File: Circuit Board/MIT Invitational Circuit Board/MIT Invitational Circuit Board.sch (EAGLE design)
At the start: 361 parts, among them IC1101 7805DT, IC1201 7805DT, IC1301 7805DT, IC1501 7805DT, J1005 ICSP_HEADER, J1104 ICSP_HEADER, J1204 ICSP_HEADER, J1304 ICSP_HEADER, J204 ICSP_HEADER, J301 ICSP_HEADER, J401 ICSP_HEADER, J503 ICSP_HEADER, J603 ICSP_HEADER, J703 ICSP_HEADER, J704 ICSP_HEADER, J903 ICSP_HEADER, Q1001 PSMN7R0-60YS, Q1401 PSMN7R0-60YS, Q201 PSMN7R0-60YS, Q301 500mA/300V, Q401 500mA/300V, Q501 PSMN7R0-60YS, Q601 PSMN7R0-60YS, Q801 PSMN7R0-60YS, Q901 PSMN7R0-60YS, U1001 ATTINY25-20SSUR, U1002 MIC5205, U101 74HC1G04, U102 MIC5205, U1101 DRV8835, U1102 ATTINY25-20SSUR, U1201 DRV8835, U1202 ATTINY25-20SSUR, U1301 DRV8835, U1302 ATTINY25-20SSUR, U1401 74HC1G04, U1402 MIC5205, U201 74HC1G04, U202 ATTINY25-20SSUR, U203 MIC5205, U301 74HC1G04, U302 SN74C1G08-DCK, U303 ATTINY25-20SSUR, U304 MIC5205, U401 74HC1G04, U402 SN74C1G08-DCK, U403 ATTINY25-20SSUR, U404 MIC5205, U501 74HC1G04, U502 SN74C1G08-DCK, U503 ATTINY25-20SSUR, U504 MIC5205, U601 74HC1G04, U602 SN74C1G08-DCK, U603 ATTINY25-20SSUR, U604 MIC5205, U701 ATTINY25-20SSUR, U702 ATTINY25-20SSUR, U703 MIC5205, U801 74HC1G04, U802 SN74C1G08-DCK, U803 MIC5205, U901 ATTINY25-20SSUR, U902 MIC5205, X1601 MSTBA2

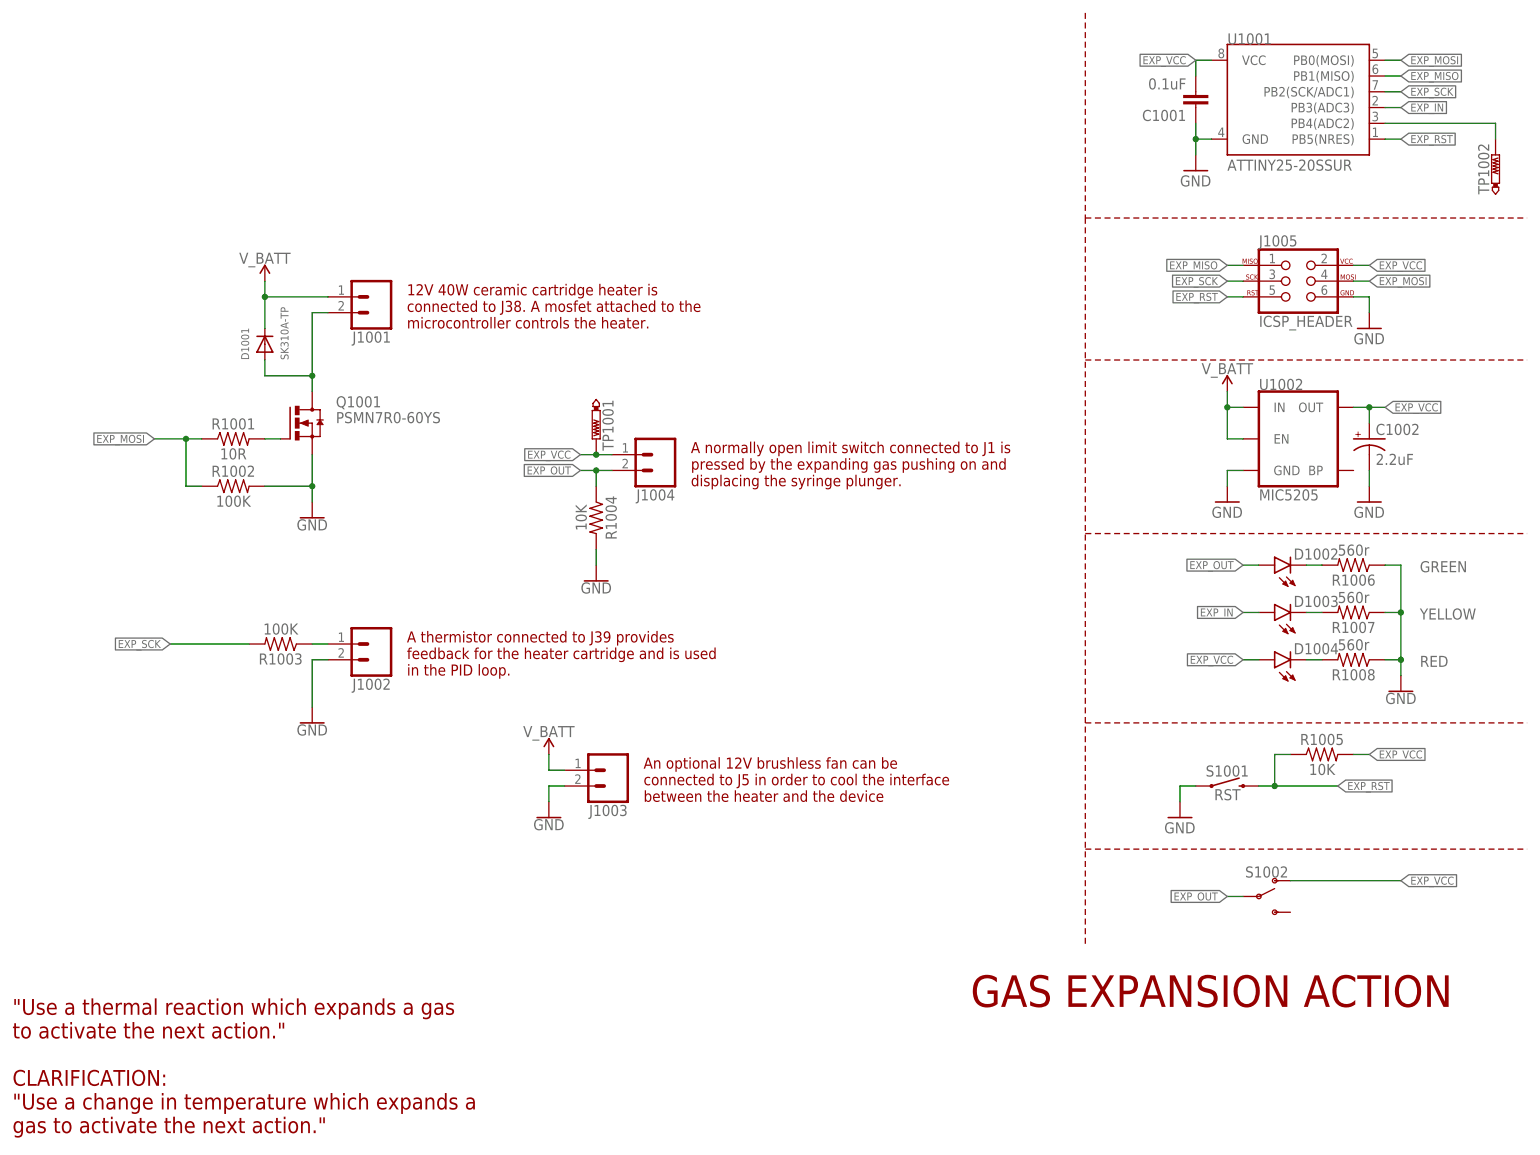
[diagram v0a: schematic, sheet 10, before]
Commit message: Reorganized files and updated schematics
MIT schematics have been finalized and the code is pretty stable, beisdes some thresholding issues.
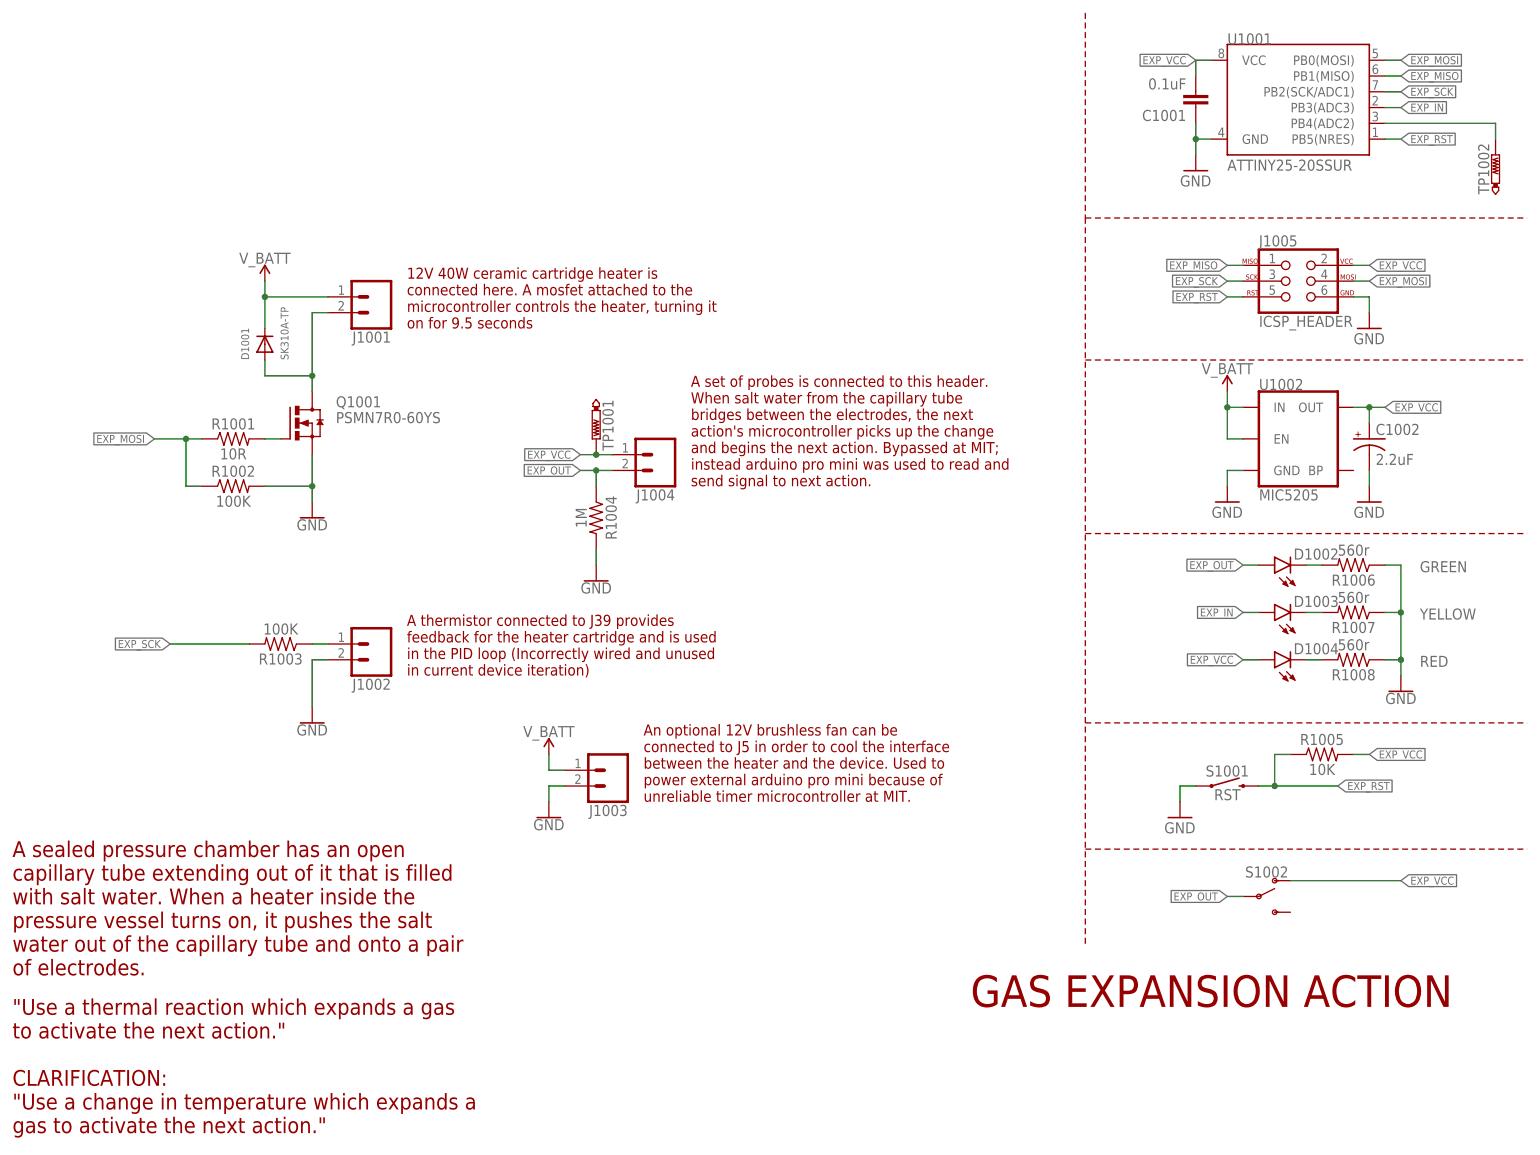
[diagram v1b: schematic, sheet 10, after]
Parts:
- R1004: value 10K -> 1M
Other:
- note added: "100uF, 25V capacitor was added following MIT invitational because of jerky motor performance. Connected between IMA7_VCC and GND on ICSP header on rear of board."
- note added: "12V 40W ceramic cartridge heater is connected here. A mosfet attached to the microcontroller controls the heater, turning it on for 9.5 seconds"
- note added: "A 12V brushless fan can be connected to to cool solenoid"
- note added: "A counterweight is released by an electromagnet, which drops and pulls up a 500g mass. The mass raises 10cm then hits a limit switch, triggering the next action."
- note added: "A motor connected here rotates, pulling the string that is connected to the mass"
- note added: "A motor connected to this header flips the pressure chamber then pulses back and forth for several seconds to ensure the alkaseltzer is mixing with the water."
- note added: "A normally open limit switch connected here is pressed by the expanding gas."
- note added: "A normally open limit switch connected here is pressed by the levers., triggering the next action."
- note added: "A normally open limit switch connected here is pressed by the mass as it lifts"
- note added: "A reed switch is connected to J801 and starts the next action when closed by the electromagnet"
- note added: "A reed switch is released by a magnet. The switch outputs a signal to begin the next transfer."
- note added: "A sealed pressure chamber has an open capillary tube extending out of it that is filled with salt water. When a heater inside the pressure vessel turns on, it pushes the salt water out of the capillary tube and onto a pair of electrodes."
- note added: "A set of probes is connected to this header. When salt water from the capillary tube bridges between the electrodes, the next action's microcontroller picks up the change and begins the next action. Bypassed at MIT; instead arduino pro mini was used to read and send signal to next action."
- note added: "A solenoid is connected. A mosfet attached to the microcontroller controls it."
- note added: "A solenoid is connected. A mosfet attached to the microcontroller controls it. After a short period of activation, the mosfet is turned off and the solenoid releases."
- note added: "A solenoid valve is connected here. A mosfet attached to the microcontroller controls the state of the valve."
- note added: "A solenoid valve is connected to J502. A mosfet attached to the microcontroller controlls the state of the valve."
- note added: "A solenoid valve is opened, releasing water into a test tube containing ammonium nitrate powder. The powder dissolves in an endothermic reaction, causing the resistance of a thermistor to change."
- note added: "A solenoid valve opens, releasing a small amount of fresh water into a test tube already containing salt water. The salt water level raises, touching two electrodes. The change in resistance is sensed by the microcontroller, which begins the next action."
- note added: "A thermistor connected to J39 provides feedback for the heater cartridge and is used in the PID loop (Incorrectly wired and unused in current device iteration)"
- note added: "A thermistor is used to check the temperature of the reaction."
- note added: "Alkaseltzer and water start uncombined in syringe becase of 3D printed "table" inside syringe which holds alkaseltzer up. Syringe flips, combining the two, and plunger slowly moves outwards."
- note added: "An IR diode recieves the LED pulses, which are then decoded by the microcontroller."
- note added: "An LED connected to the first microcontroller pulses out a certain sequence of pulses."
- note added: "An electromagnet is connected to this header. The electromagnet deactivates, dropping a counterweight."
- note added: "An inductive NPN proximity sensor is connected to and read by the microcontroller"
- note added: "An optional 12V brushless fan can be connected to J5 in order to cool the interface between the heater and the device. Used to power external arduino pro mini because of unreliable timer microcontroller at MIT."
- note added: "DO NOT POPULATE"
- note added: "Incandescent bulb, not LED"
- note added: "Output is not normally inverted, can be inverted if error is made in function."
- note added: "Power and Inter-Action"
- note added: "Previous transfer triggers DFrobot sound recording module (connected to J6), which then plays the end recording."
- note added: "Resistance of saltwater is monitored by split contacts plugged in here"
- note added: "Revision Jan 2018: Add 10K resistor to back of PCB between ICSP pins SCK and VCC on this action only (nets ENDO_SCK and ENDO_VCC). Voltage divider resistor was improperly placed."
- note added: "Revision January 2018: Connect TP802 and TP801, and do not populate U801. This eliminates jittery reed switch action, but leaves the electromagnet on. Problem mitigated by change to IR reciever code."
- note added: "Syringe with baking soda filled basket attached to plunger is filled with 30% warm vinegar. When syringe is flipped, the two react and the resulting reaction inflates a balloon which hits a limit switch 20cm away."
- note added: "The pulley system, powered by the motor, lifts a mass up 10cm and hits two limit switches, one turns off the motor and the other triggers the next action."
- note removed: "12V 40W ceramic cartridge heater is connected to J38. A mosfet attached to the microcontroller controls the heater."
- note removed: "A motor connected to J41 rotates, pulling the string that is connected to the mass"
- note removed: "A motor connected to J54 flips the pressure chamber then pulses back and forth for several seconds to ensure the alkaseltzer is mixing with the water."
- note removed: "A normally open limit switch connected to J1 is pressed by the expanding gas pushing on and displacing the syringe plunger."
- note removed: "A normally open limit switch connected to J42 is pressed by the mass as it lifts"
- note removed: "A normally open limit switch connected to J53 is pressed by the levers."
- note removed: "A normally open limit switch connected to J55 is pressed by the expanding gas."
- note removed: "A reed switch is released by a magnet. The attached microcontroller detects the change and outputs a signal to begin the next transfer."
- note removed: "A solenoid is connected to J50. A mosfet attached to the microcontroller controls it. After a short period of activation, the mosfet is turned off and the solenoid releases."
- note removed: "A solenoid is connected to J51. A mosfet attached to the microcontroller controls it."
- note removed: "A solenoid valve is connected to J3. A mosfet attached to the microcontroller controlls the state of the valve."
- note removed: "A solenoid valve is connected to J45. A mosfet attached to the microcontroller controlls the state of the valve."
- note removed: "A thermistor connected to J2 is used to check the temperature of the reaction."
- note removed: "A thermistor connected to J39 provides feedback for the heater cartridge and is used in the PID loop."
- note removed: "An IR diode recieves the LED pulses and signals rom the LED, which are then decoded by the microcontroller."
- note removed: "An LED connected to the first microcontroller pulses out a TV remote signal."
- note removed: "An electromagnet is connected to this header. The electromagnet deactivates, dropping a conterweight."
- note removed: "An inductive NPN proximity sensor is connected to J52. It is read by the microcontroller."
- note removed: "An optional 12V brushless fan can be connected to J5 in order to cool the interface between the heater and the device"
- note removed: "An optional 12V brushless fan can be connected to J56 in order to cool the solenoid"
- note removed: "Halogen bulb (not LED) - do we need a back voltage diode?"
- note removed: "Non-action Components"
- note removed: "Previous transfer triggers sound recoring module (connected to J6), which then plays the end recording."
- note removed: "Resistance of saltwater is monitored by split contacts plugged into header J46"
- note removed: "https://www.amazon.com/uxcell-Electric-Lifting-Electromagnet-Solenoid/dp/B01N3387AA/ref=sr_1_4?ie=UTF8&qid=1513817515&sr=8-4&keywords=electromagnet&th=1"
- note removed: "https://www.ebay.com/itm/DC12V-2A-20N-10mm-Pull-Push-Type-Linear-Motion-Solenoid-Electromagnet-/ 253056280056?_trksid=p2349526.m4383.l4275.c1"
- moved on the sheet: JP201
